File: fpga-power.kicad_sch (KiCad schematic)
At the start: 73 parts, among them U1 XC7K70T-FBG484

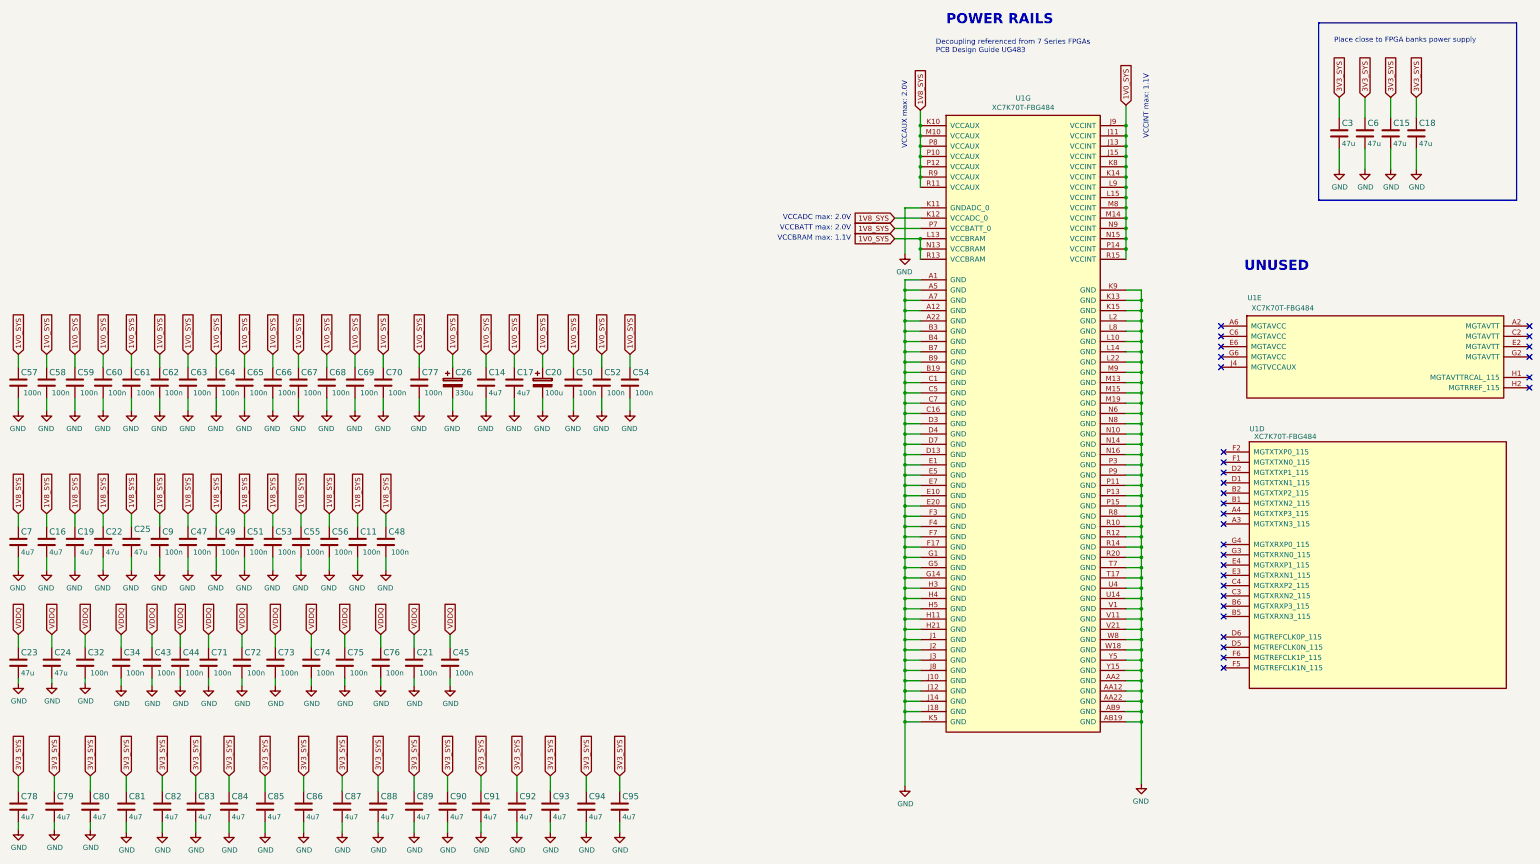
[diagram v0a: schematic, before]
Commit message: Placement and routing of FT4232H. Re annotation of the schematics
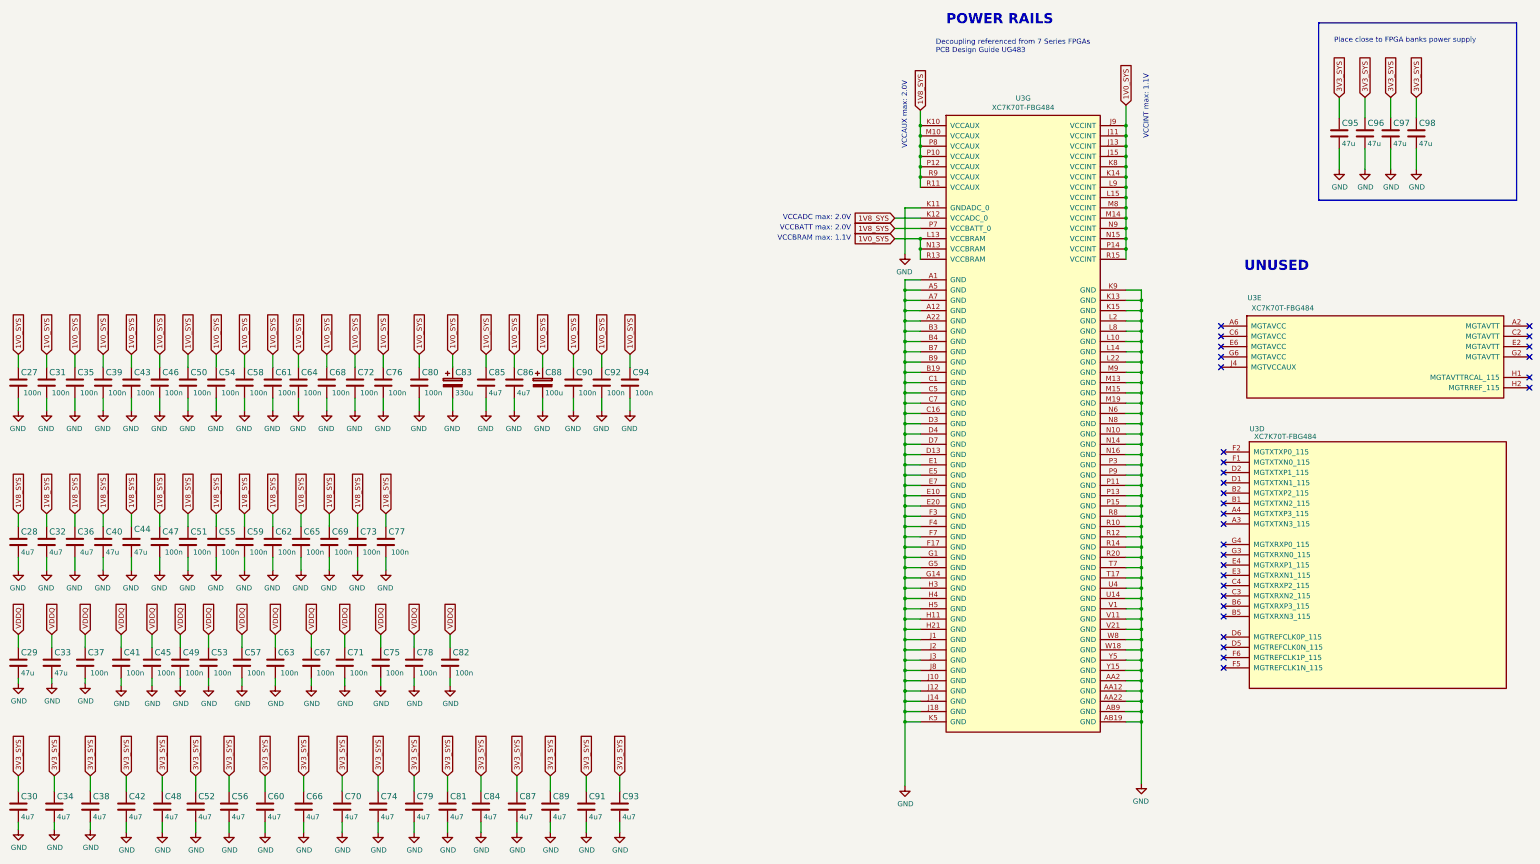
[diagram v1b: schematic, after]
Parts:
- renumbered C57 to C27, C7 to C28, C23 to C29, C78 to C30, C58 to C31, C16 to C32, C24 to C33, C79 to C34, C59 to C35, C19 to C36, C32 to C37, C80 to C38, C60 to C39, C22 to C40, C34 to C41, C81 to C42, C61 to C43, C25 to C44, C43 to C45, C62 to C46, C9 to C47, C82 to C48, C44 to C49, C63 to C50, C47 to C51, C83 to C52, C71 to C53, C64 to C54, C49 to C55, C84 to C56, C72 to C57, C65 to C58, C51 to C59, C85 to C60, C66 to C61, C53 to C62, C73 to C63, C67 to C64, C55 to C65, C86 to C66, C74 to C67, C56 to C69, C87 to C70, C75 to C71, C69 to C72, C11 to C73, C88 to C74, C76 to C75, C70 to C76, C48 to C77, C21 to C78, C89 to C79, C77 to C80, C90 to C81, C45 to C82, C26 to C83, C91 to C84, C14 to C85, C17 to C86, C92 to C87, C20 to C88, C93 to C89, C50 to C90, C94 to C91, C52 to C92, C95 to C93, C54 to C94, C3 to C95, C6 to C96, C15 to C97, C18 to C98, U1 to U3

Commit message: Add 3d model of DDR5 testbed. Fix annotation
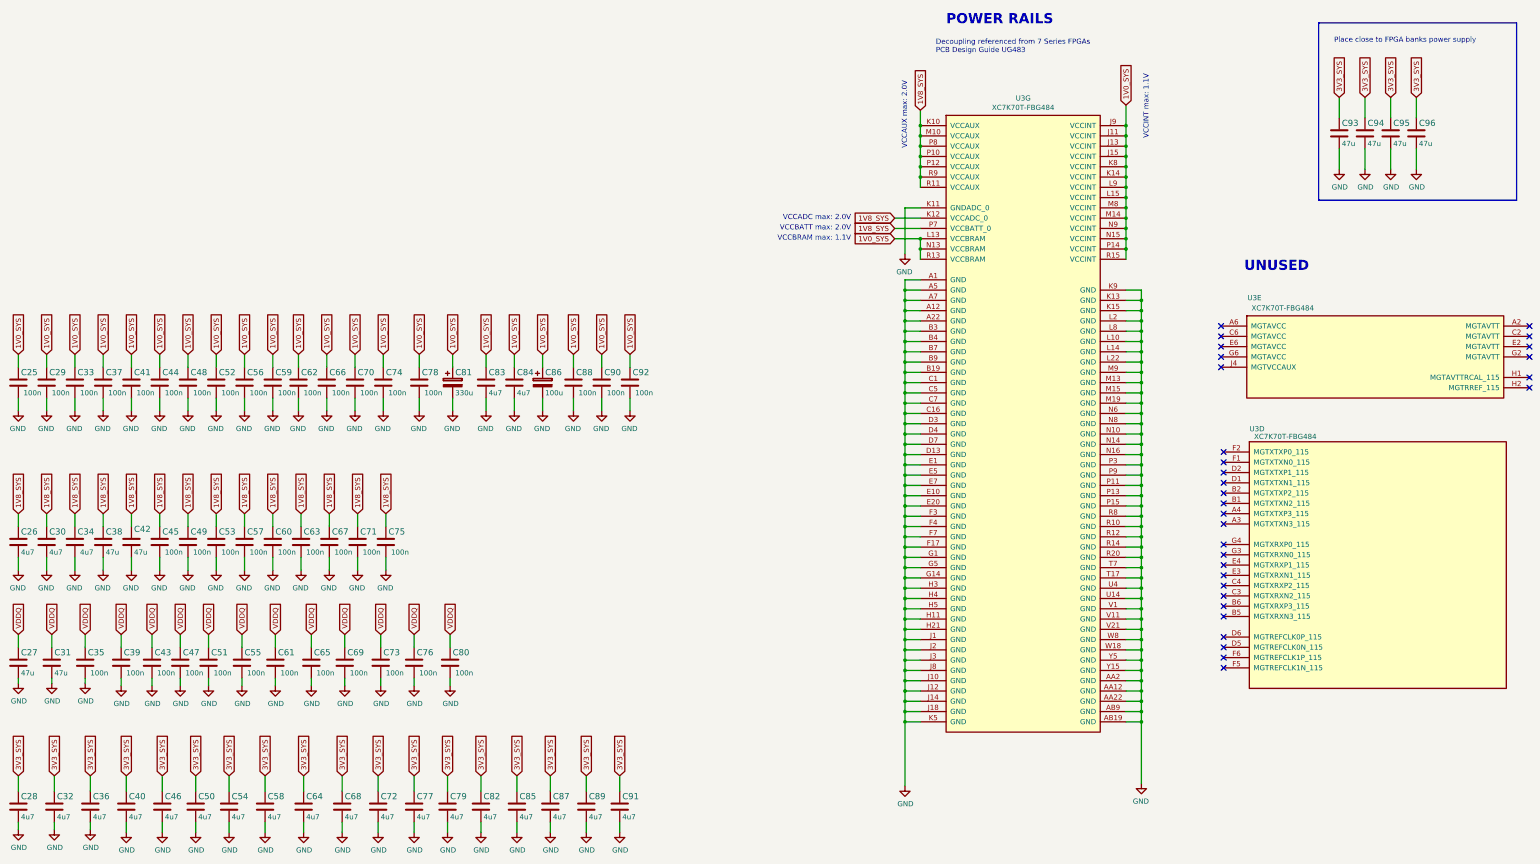
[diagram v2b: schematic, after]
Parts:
- renumbered C27 to C25, C28 to C26, C29 to C27, C30 to C28, C31 to C29, C32 to C30, C33 to C31, C34 to C32, C35 to C33, C36 to C34, C37 to C35, C38 to C36, C39 to C37, C40 to C38, C41 to C39, C42 to C40, C43 to C41, C44 to C42, C45 to C43, C46 to C44, C47 to C45, C48 to C46, C49 to C47, C50 to C48, C51 to C49, C52 to C50, C53 to C51, C54 to C52, C55 to C53, C56 to C54, C57 to C55, C58 to C56, C59 to C57, C60 to C58, C61 to C59, C62 to C60, C63 to C61, C64 to C62, C65 to C63, C66 to C64, C67 to C65, C68 to C66, C69 to C67, C70 to C68, C71 to C69, C72 to C70, C73 to C71, C74 to C72, C75 to C73, C76 to C74, C77 to C75, C78 to C76, C79 to C77, C80 to C78, C81 to C79, C82 to C80, C83 to C81, C84 to C82, C85 to C83, C86 to C84, C87 to C85, C88 to C86, C89 to C87, C90 to C88, C91 to C89, C92 to C90, C93 to C91, C94 to C92, C95 to C93, C96 to C94, C97 to C95, C98 to C96
